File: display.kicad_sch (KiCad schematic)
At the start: 44 parts, among them Q3 SSM6N35AFE, Q4 SSM6N35AFE

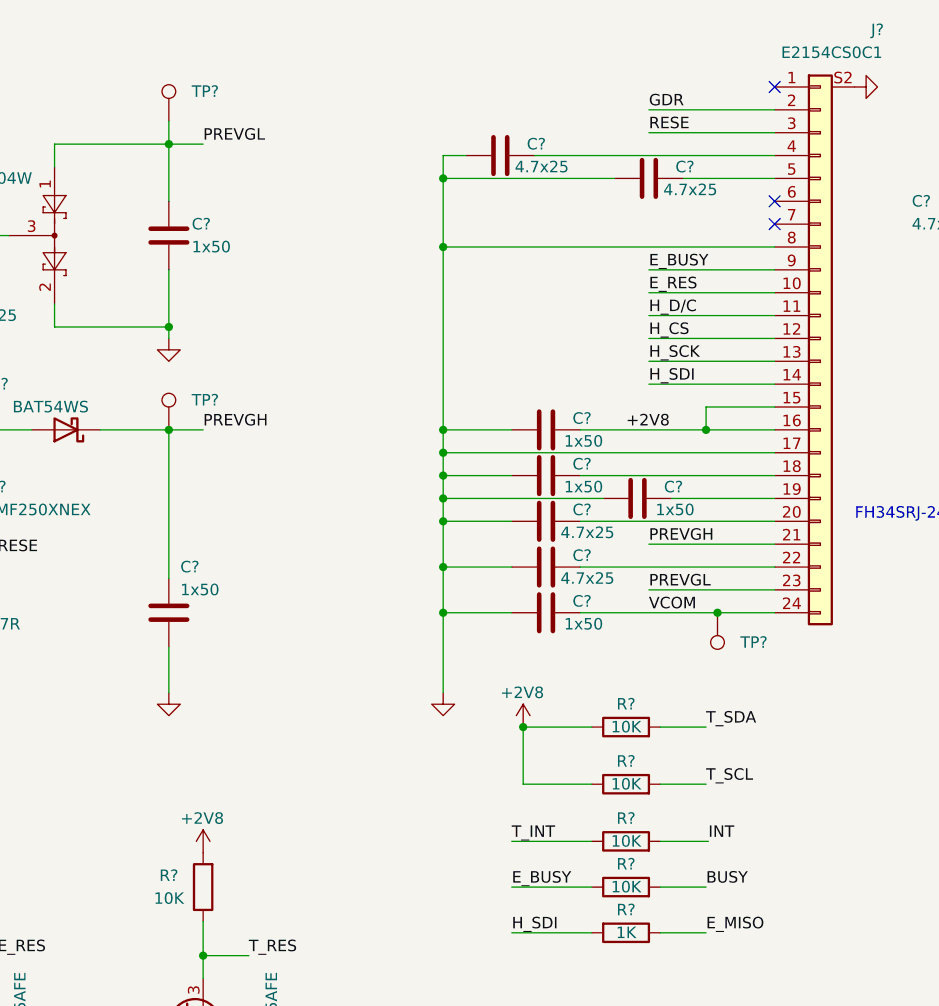
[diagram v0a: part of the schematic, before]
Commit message: G2 revision
G2 revision = Kampela development kit

Features:
- electronics is more stable and reliable
- better power harvesting efficiency
- fixed a touchscreen instability with powerful NFC transmitters
- mechanical layout improved for low-volume productions for a devkit batch
- NFC coil placed closer to the phone antenna. The coil parameters are optimized based on a mathematical model of the NFS harvester circuit.
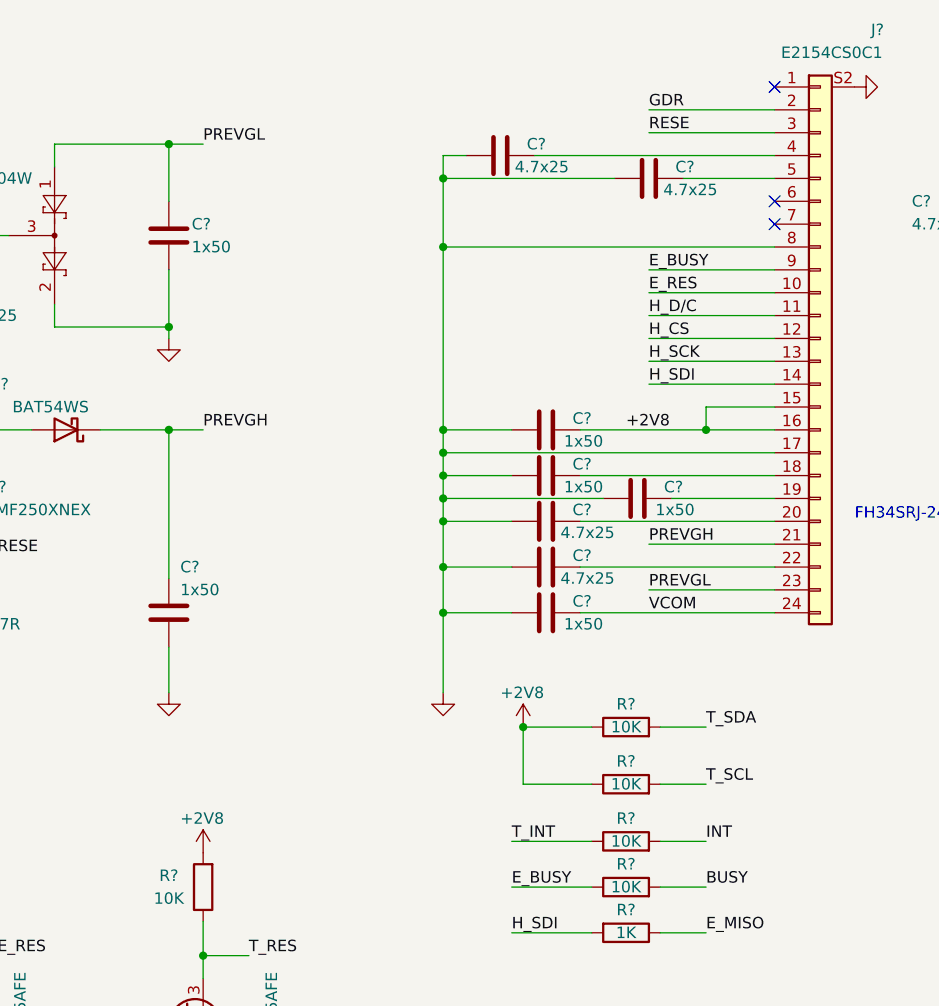
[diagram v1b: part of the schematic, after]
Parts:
- removed TP? (x3): TestPoint, TestPoint:TestPoint_Pad_D1.0mm, symbol Connector:TestPoint

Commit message: G5 revision
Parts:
- added TP? (x12): TestPoint, TestPoint:TestPoint_Pad_D1.0mm, symbol Connector:TestPoint
- C? (x3): value 1x50 -> 1x6.3
- C? (x6): footprint Capacitor_SMD:C_0402_1005Metric -> Capacitor_SMD:C_0603_1608Metric
- C?: value 4.7x25 -> 1x6.3
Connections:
- net E_BUSY: now also TP?.1
- net E_RES: now also TP?.1
- net H_CS: now also TP?.1
- net H_D/C: now also TP?.1
- net H_SCK: now also TP?.1
- net H_SDI: now also TP?.1
- net PREVGH: now also TP?.1
- net PREVGL: now also TP?.1
- net T_INT: now also TP?.1
- net T_SCL: now also TP?.1
- net T_SDA: now also TP?.1
- net VCOM: now also TP?.1
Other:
- moved on the sheet: C?

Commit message: Next revision
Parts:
- removed C? (x4): 1x6.3, Capacitor_SMD:C_0402_1005Metric, symbol Device:C
- removed C? (x6): 4.7x25, Capacitor_SMD:C_0603_1608Metric, symbol Device:C
- removed C? (x3): 1x50, Capacitor_SMD:C_0402_1005Metric, symbol Device:C
- removed C?: 0.1, Capacitor_SMD:C_0402_1005Metric, symbol Device:C
- removed C? (x3): 0.1u, Capacitor_SMD:C_0402_1005Metric, symbol Device:C
- removed D?: BAT54WS, Diode_SMD:D_SOD-323F, symbol Device:D_Schottky
- removed D?: BAS70-04W, Package_TO_SOT_SMD:SOT-323_SC-70, symbol Diode:BAT54SW
- removed FB?: BLM18KG102SN1D, Inductor_SMD:L_0603_1608Metric, symbol Device:FerriteBead_Small
- removed J?: E2154CS0C1, MyLib:GDEY027T91-T01_bended, symbol Connector_Generic:Conn_01x24
- removed L?: NR3015T100M, Inductor_SMD:L_Wuerth_MAPI-3015, symbol Device:L
- removed Q4: SSM6N35AFE, Package_TO_SOT_SMD:SOT-563, symbol Transistor_FET:FDG1024NZ
- removed Q?: PMF250XNEX, Package_TO_SOT_SMD:SOT-323_SC-70, symbol Device:Q_NMOS_GSD
- removed R? (x8): 10K, Resistor_SMD:R_0402_1005Metric, symbol Device:R
- removed R? (x3): 1K, Resistor_SMD:R_0402_1005Metric, symbol Device:R
- removed R?: 470K, Resistor_SMD:R_0402_1005Metric, symbol Device:R
- removed R?: 100, Resistor_SMD:R_0402_1005Metric, symbol Device:R
- removed R?: 0.47R, Resistor_SMD:R_0603_1608Metric, symbol Device:R
- removed TP? (x9): TestPoint, TestPoint:TestPoint_Pad_D1.0mm, symbol Connector:TestPoint
- added C47, C48, C52: 0.1, Capacitor_SMD:C_0201_0603Metric, symbol Device:C
- added C49, C50: 22x6.3, Capacitor_SMD:C_0603_1608Metric, symbol Device:C
- added C51, C53: 1x6.3, Capacitor_SMD:C_0402_1005Metric, symbol Device:C
- added D6: BAT54AW, MyLib:SOT-523, symbol Diode:BAT54AW
- added J5: FPC 10 TE1-2328702-0, MyLib:TE_123287020, symbol MyLib:FPC 10 TE1-2328702-0
- added R19, R20, R22, R23: 100K, Resistor_SMD:R_0201_0603Metric, symbol Device:R
- added R21: 1M, Resistor_SMD:R_0201_0603Metric, symbol Device:R
- added R24, R25, R26, R27, R28: 10K, Resistor_SMD:R_0201_0603Metric, symbol Device:R
- added TP16, TP17, TP18, TP19, TP20, TP21, TP22: TestPoint, TestPoint:TestPoint_Pad_D1.0mm, symbol Connector:TestPoint
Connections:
- net 2V8_EN is gone; now on net +3V0: Q3.2 (G), Q3.5 (G)
- net T_RES is gone; now on net +3V0: J?.3 (Pin_3)
- net +1V8: now also U?.12 (OE), C47.1
- net GND: now also C47.2, C48.2, C49.1, C50.1, C51.2, C52.1, C53.2, J5.1, J5.2, J5.MP1, J5.MP2, R19.1, R20.1, R22.1, R23.1
- net H_CS: now also J5.8, R22.2, TP19.1
- net H_SCK: now also U?.10 (B1), J5.10, R19.2, TP21.1; no longer U?.9 (B2)
- net H_SDI: now also U?.9 (B2), J5.9, R20.2, TP20.1
- net INT: now also R28.1
- net SCK: now also U?.2 (A1); no longer U?.3 (A2)
- net SCL: now also R25.1
- net SDA: now also R24.1
- net SDI: now also U?.3 (A2); no longer U?.2 (A1)
- net T_INT: now also R28.2
- net T_SCL: now also R27.1
- net T_SDA: now also R26.1
- net +2V8 renamed +3V0
- net +3V0: now also C48.1, C52.2, C53.1, R24.2, R25.2, R26.2, R27.2, TP22.1; no longer U?.12 (OE)
- net D/C renamed EXTIN
- net H_D/C renamed H_EXTIN
- net H_EXTIN: now also J5.7, R23.2, TP18.1
- new net: C51.1, J5.6, R21.1, TP17.1
- new net: C49.2, C50.2, D6.2, J5.3, J5.4, J5.5, TP16.1
- new net: D6.1, R21.2
- new net +5V: D6.3
- no-connect marks 3 -> 0
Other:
- note removed: "FH34SRJ-24S-0.5SH"
- moved on the sheet: J?, Q3A, Q3B, TP?, U?
